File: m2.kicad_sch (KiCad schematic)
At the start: 4 parts, among them J2 Bus_M.2_Socket_M, Y1 SG-3030CM

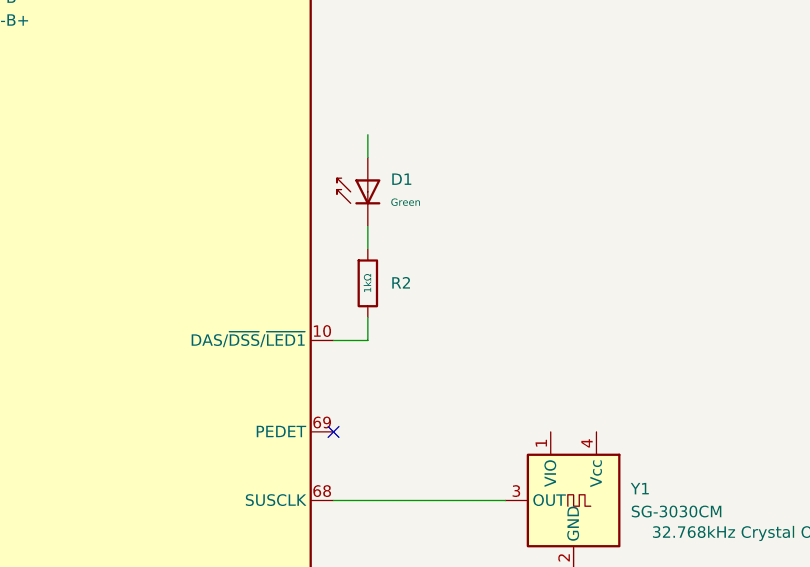
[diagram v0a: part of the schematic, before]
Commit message: [#1] WIP: Change components to ones from the global library, refactor schematic
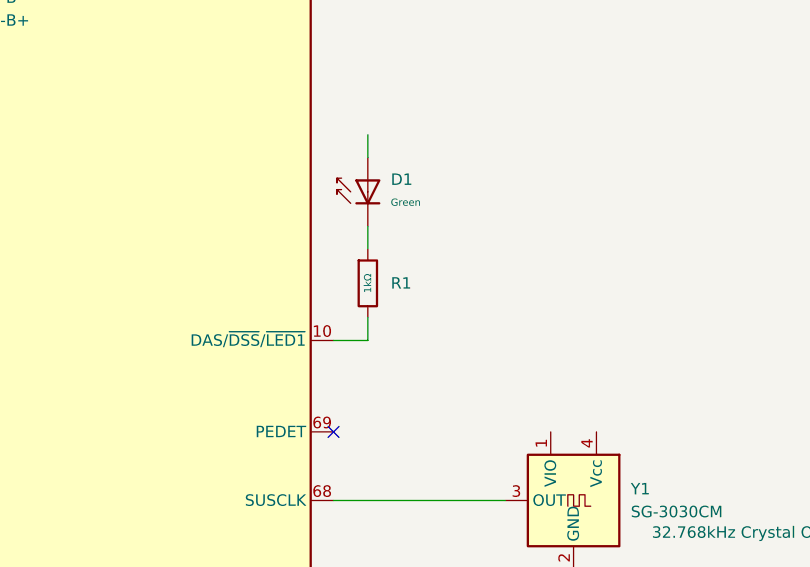
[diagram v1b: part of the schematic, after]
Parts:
- renumbered R2 to R1
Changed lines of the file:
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@@
 		(on_board yes)
 		(dnp no)
-		(property "Reference" "#PWR040"
+		(property "Reference" "#PWR017"
 			(at 262.89 184.15 0)
 			(effects
@@
 			(project "cm5-module"
 				(path "/090a8e41-87a8-4fb1-998b-60a2c0dc4cee/18a4552b-ac02-46c8-954e-f58b32a322f0"
-					(reference "#PWR040")
+					(reference "#PWR017")
 					(unit 1)
 				)
@@
 		(on_board yes)
 		(dnp no)
-		(property "Reference" "#PWR039"
+		(property "Reference" "#PWR018"
 			(at 210.82 195.58 0)
 			(effects
@@
 			(project "cm5-module"
 				(path "/090a8e41-87a8-4fb1-998b-60a2c0dc4cee/18a4552b-ac02-46c8-954e-f58b32a322f0"
-					(reference "#PWR039")
+					(reference "#PWR018")
 					(unit 1)
 				)
@@
 		(dnp no)
 		(fields_autoplaced yes)
-		(property "Reference" "R2"
+		(property "Reference" "R1"
 			(at 242.57 142.2399 0)
 			(effects
@@
 			(project ""
 				(path "/090a8e41-87a8-4fb1-998b-60a2c0dc4cee/18a4552b-ac02-46c8-954e-f58b32a322f0"
-					(reference "R2")
+					(reference "R1")
 					(unit 1)
 				)
